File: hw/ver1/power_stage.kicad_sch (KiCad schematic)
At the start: 1 part, among them U3 74HC4051

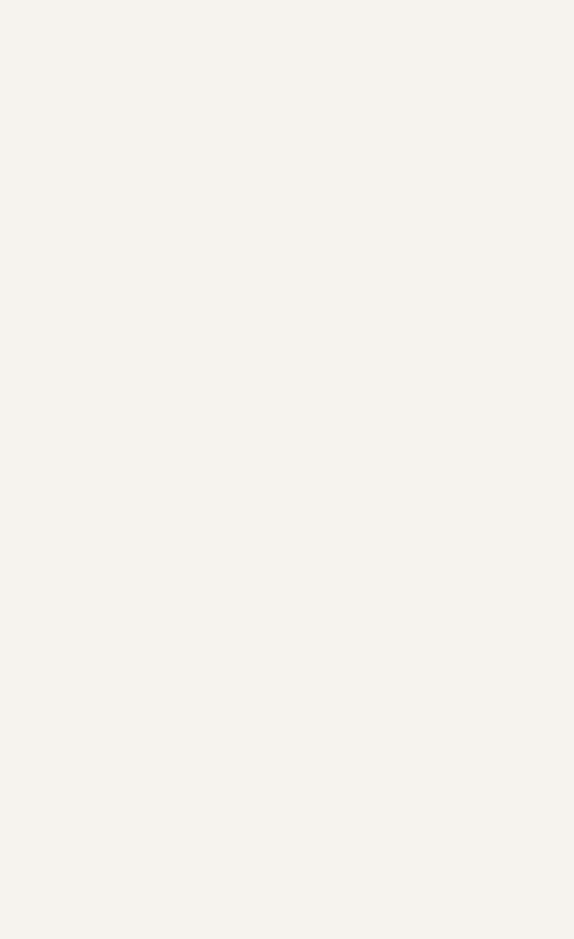
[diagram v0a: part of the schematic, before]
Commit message: Add virtual environment. Layout some schematic ideas. Add design doc for LTC7871.
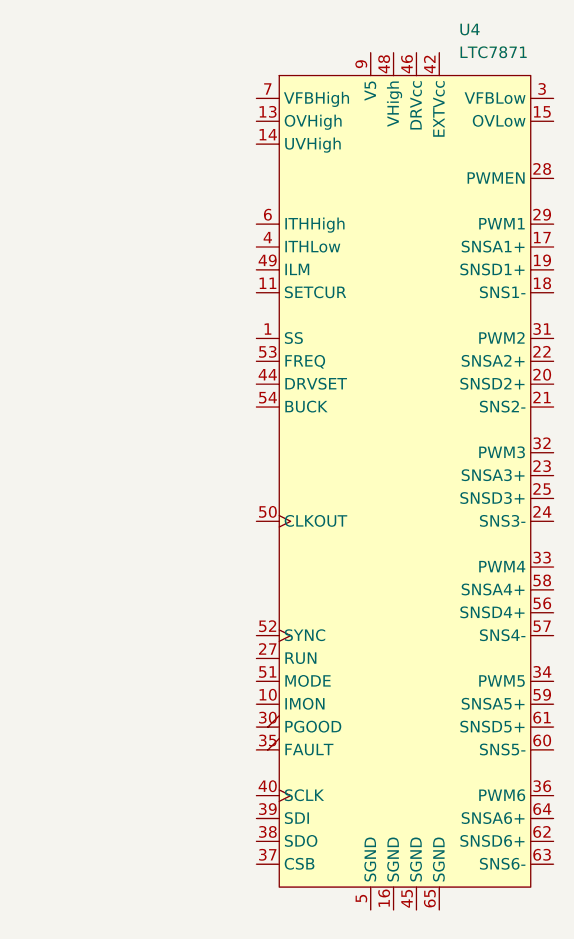
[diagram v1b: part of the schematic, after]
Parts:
- added U4: LTC7871, Package_QFP:LQFP-64-1EP_10x10mm_P0.5mm_EP6.5x6.5mm_ThermalVias, symbol ltc7871:LTC7871xLWE#xPBF

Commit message: Save the day's effort
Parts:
- added C1: 10uF, symbol Device:C
- added JP1: SolderJumper_2_Bridged, Jumper:SolderJumper-2_P1.3mm_Bridged_RoundedPad1.0x1.5mm, symbol Jumper:SolderJumper_2_Bridged
- added JP2: Jumper_3_Open, Jumper:SolderJumper-3_P1.3mm_Open_RoundedPad1.0x1.5mm_NumberLabels, symbol Jumper:Jumper_3_Open
- added R1: 1k, Resistor_SMD:R_0603_1608Metric, symbol Device:R_US
- added R2: 10k, Resistor_SMD:R_0603_1608Metric, symbol Device:R_US
- added TP1: TestPoint_Small, symbol Connector:TestPoint_Small
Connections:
- net GND: now reaches U4.16 (SGND)
- net GND: now also U4.45 (SGND), U4.5 (SGND), U4.65 (SGND), C1.2
- net LTC_RUN: now reaches U4.27 (RUN)
- net LTC_RUN: now also JP1.2 (B)
- net LTC_MODE: now reaches U4.51 (MODE)
- net LTC_MODE: now also JP2.2 (C)
- net +5P: now reaches U4.9 (V5)
- net +5P: now also C1.1, JP2.3 (B)
- new net: JP1.1 (A), R1.2, R2.2
- new net CTL_RUN: R1.1
- new net GNDD: JP2.1 (A), R2.1
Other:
- note added: "+5V == Discontinuous Mode GND == Forced Continuous Mode FLT == Burst Mode"

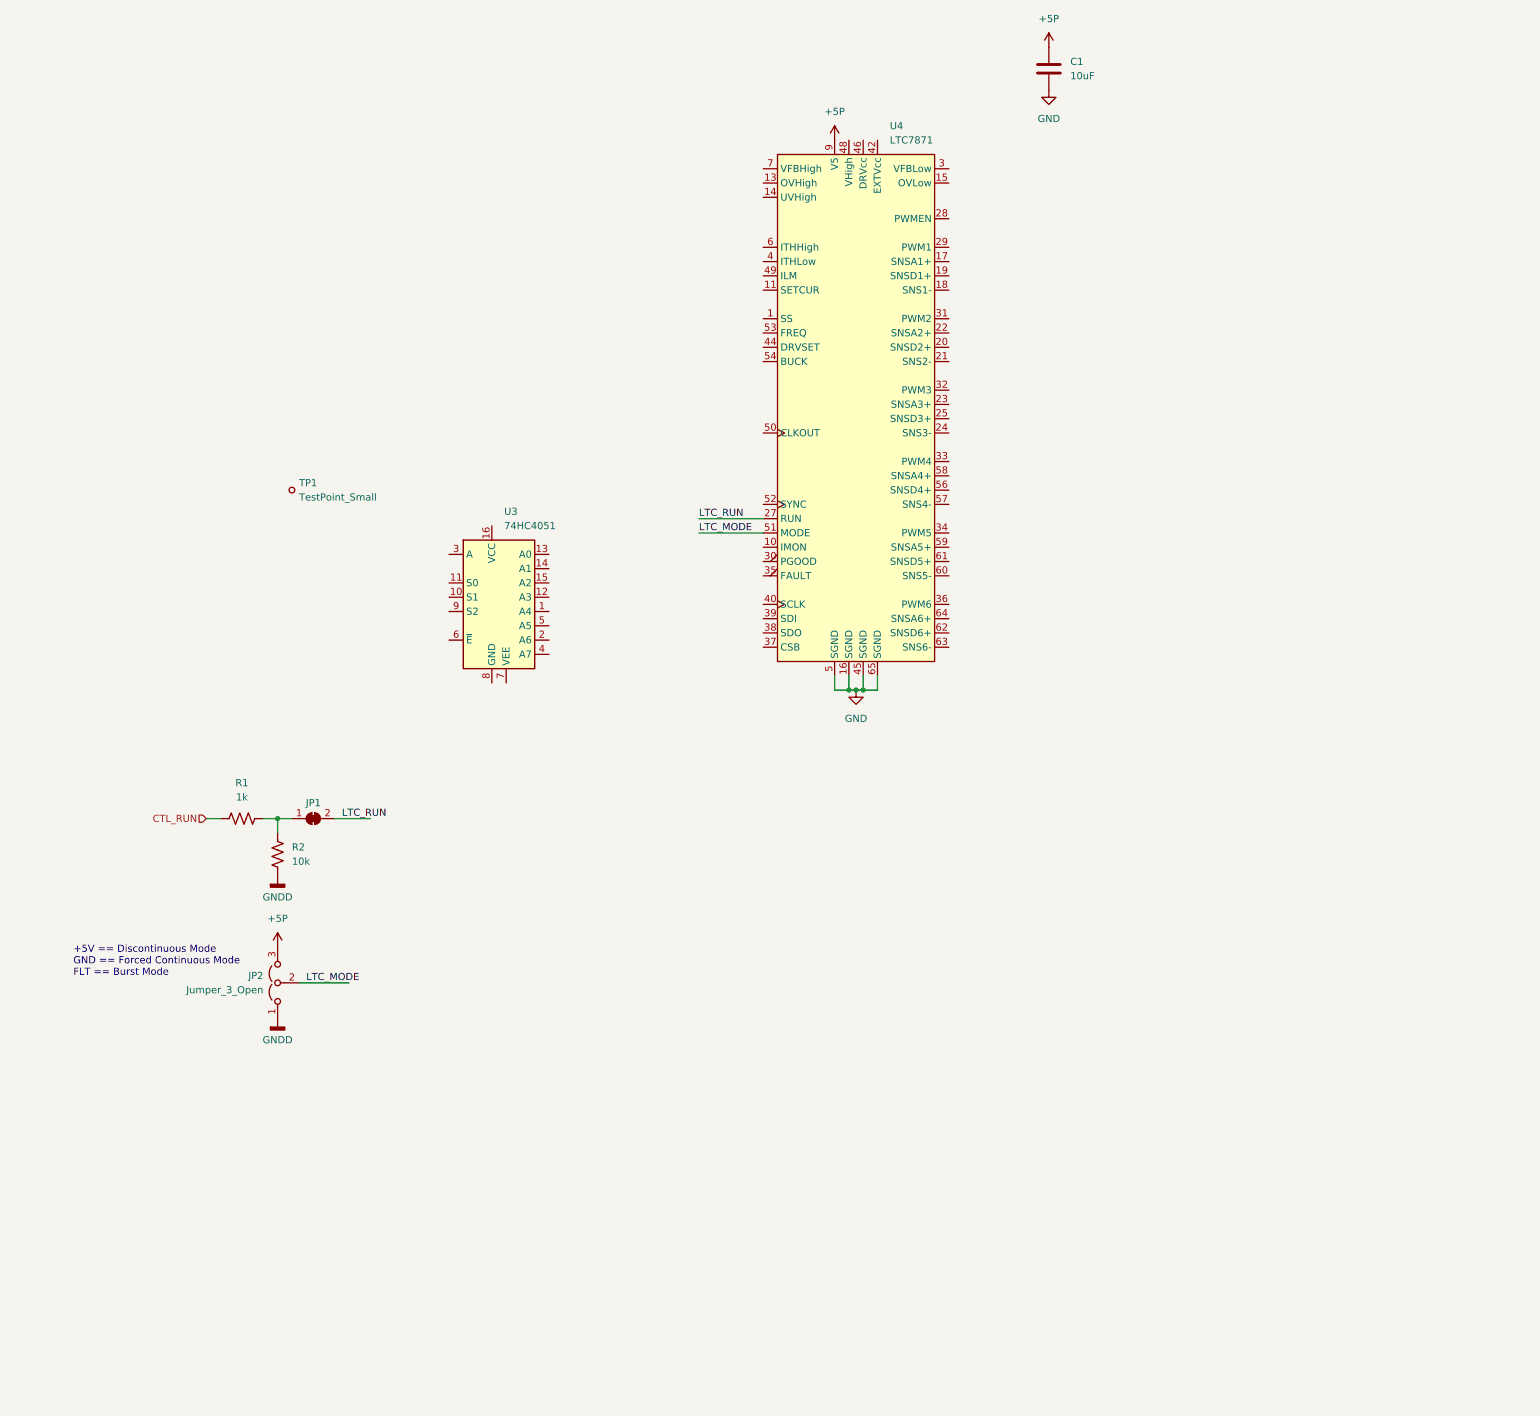
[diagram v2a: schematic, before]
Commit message: Flesh out some more of the power design
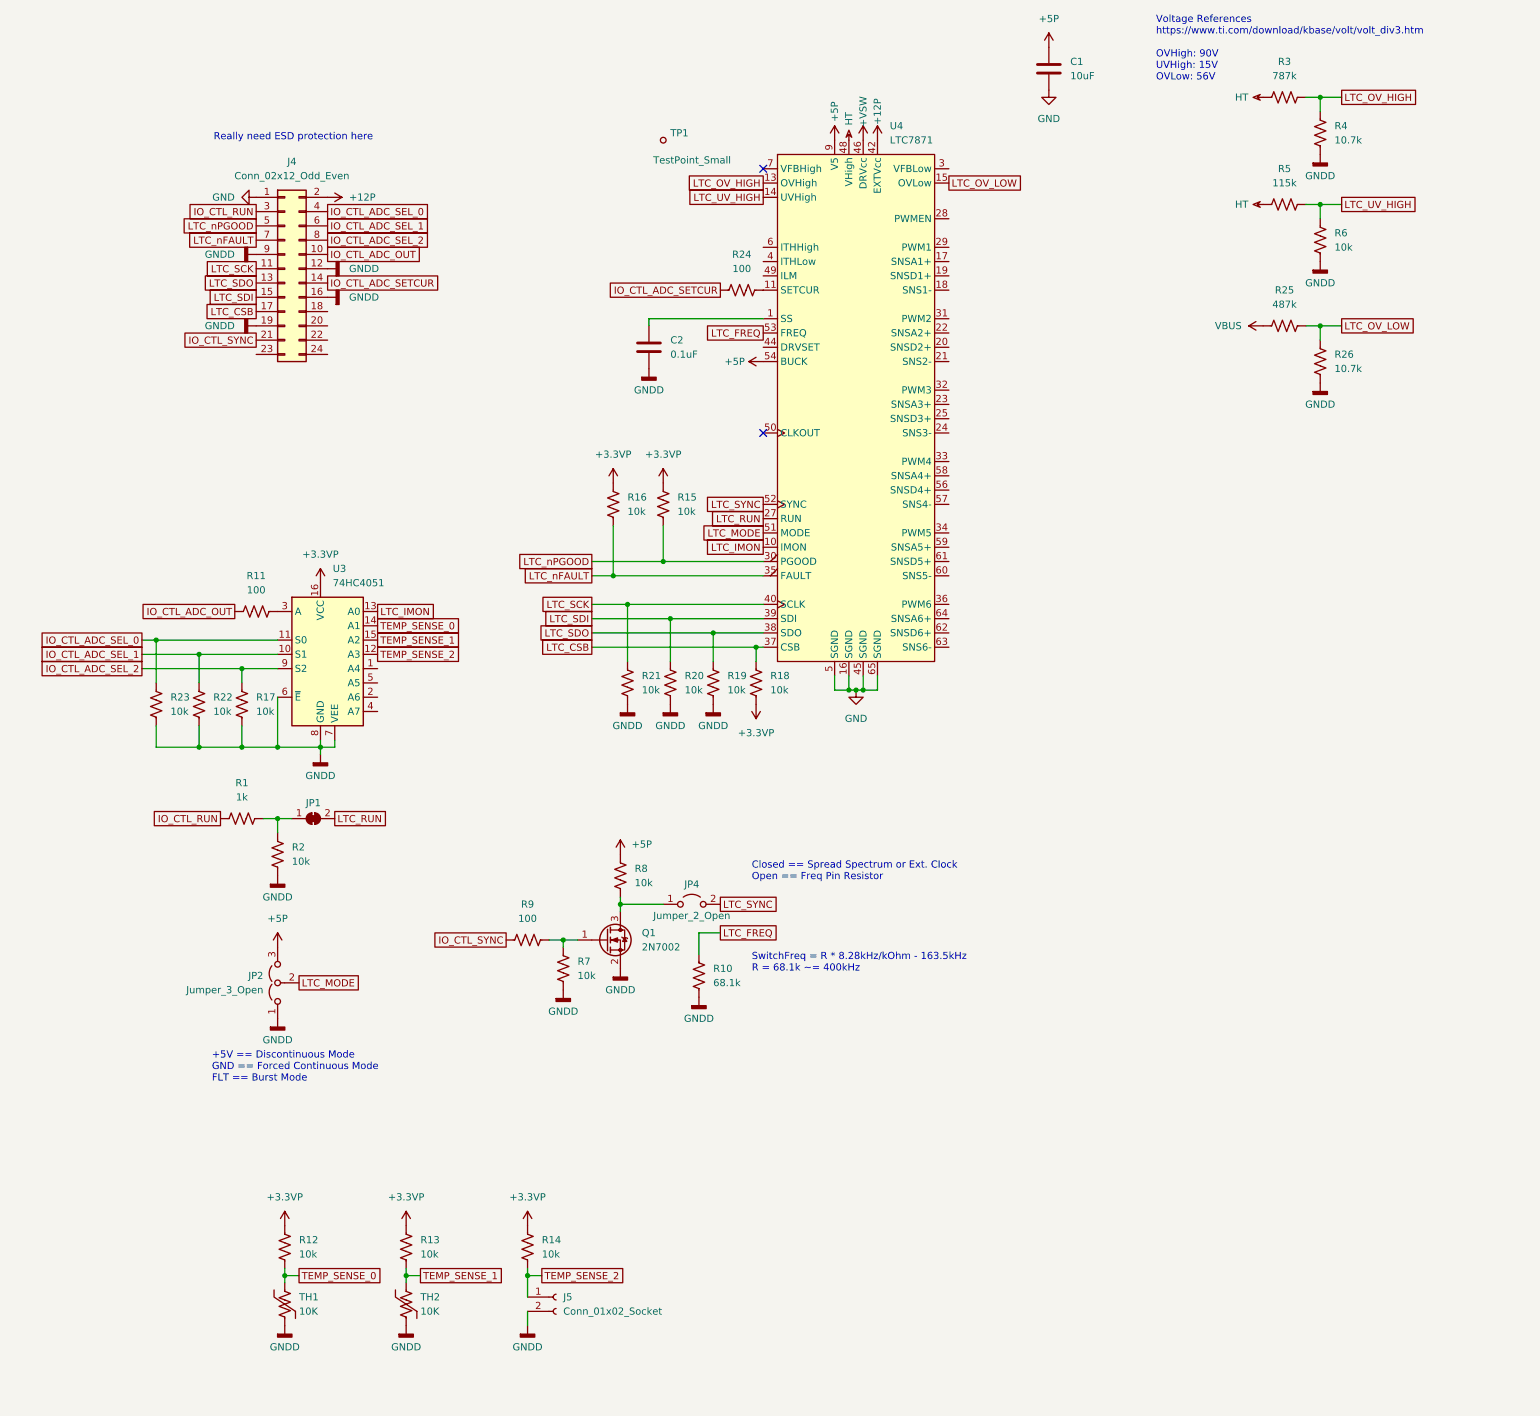
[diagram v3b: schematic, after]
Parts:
- added C2: 0.1uF, symbol Device:C
- added J4: Conn_02x12_Odd_Even, symbol Connector_Generic:Conn_02x12_Odd_Even
- added J5: Conn_01x02_Socket, symbol Connector:Conn_01x02_Socket
- added JP4: Jumper_2_Open, symbol Jumper:Jumper_2_Open
- added Q1: 2N7002, Package_TO_SOT_SMD:SOT-23, symbol Transistor_FET:2N7002
- added R10: 68.1k, Resistor_SMD:R_0603_1608Metric, symbol Device:R_US
- added R11, R24, R9: 100, Resistor_SMD:R_0603_1608Metric, symbol Device:R_US
- added R12, R13, R14, R15, R16, R17, R18, R19, R20, R21, R22, R23, R6, R7, R8: 10k, Resistor_SMD:R_0603_1608Metric, symbol Device:R_US
- added R25: 487k, Resistor_SMD:R_0603_1608Metric, symbol Device:R_US
- added R26, R4: 10.7k, Resistor_SMD:R_0603_1608Metric, symbol Device:R_US
- added R3: 787k, Resistor_SMD:R_0603_1608Metric, symbol Device:R_US
- added R5: 115k, Resistor_SMD:R_0603_1608Metric, symbol Device:R_US
- added TH1, TH2: 10K, symbol Device:Thermistor_US
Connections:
- net +5P: now also U4.54 (BUCK), R8.2
- net GND: now also J4.1 (Pin_1)
- net GNDD: now also U3.6 (~{E}), U3.7 (VEE), U3.8 (GND), C2.2, J4.12 (Pin_12), J4.16 (Pin_16), J4.19 (Pin_19), J4.9 (Pin_9), J5.2 (Pin_2), Q1.2 (S), R10.1, R17.1, R19.1, R20.1, R21.1, R22.1, R23.1, R26.1, R4.1, R6.1, R7.1, TH1.2, TH2.2
- net IO_CTL_ADC_SEL_1: now reaches U3.10 (S1)
- net IO_CTL_ADC_SEL_1: now also J4.6 (Pin_6), R22.2
- net IO_CTL_ADC_SEL_0: now reaches U3.11 (S0)
- net IO_CTL_ADC_SEL_0: now also J4.4 (Pin_4), R23.2
- net TEMP_SENSE_2: now reaches U3.12 (A3)
- net TEMP_SENSE_2: now also J5.1 (Pin_1), R14.1
- net LTC_IMON: now reaches U3.13 (A0)
- net LTC_IMON: now also U4.10 (IMON)
- net TEMP_SENSE_0: now reaches U3.14 (A1)
- net TEMP_SENSE_0: now also R12.1, TH1.1
- net TEMP_SENSE_1: now reaches U3.15 (A2)
- net TEMP_SENSE_1: now also R13.1, TH2.1
- net +3.3VP: now reaches U3.16 (VCC)
- net +3.3VP: now also R12.2, R13.2, R14.2, R15.2, R16.2, R18.1
- net at U3.3 (A): now also R11.2
- net IO_CTL_ADC_SEL_2: now reaches U3.9 (S2)
- net IO_CTL_ADC_SEL_2: now also J4.8 (Pin_8), R17.2
- net at U4.1 (SS): now also C2.1
- net at U4.11 (SETCUR): now also R24.2
- net LTC_OV_HIGH: now reaches U4.13 (OVHigh)
- net LTC_OV_HIGH: now also R3.2, R4.2
- net LTC_UV_HIGH: now reaches U4.14 (UVHigh)
- net LTC_UV_HIGH: now also R5.2, R6.2
- net LTC_OV_LOW: now reaches U4.15 (OVLow)
- net LTC_OV_LOW: now also R25.2, R26.2
- net LTC_nPGOOD: now reaches U4.30 (PGOOD)
- net LTC_nPGOOD: now also J4.5 (Pin_5), R15.1
- net LTC_nFAULT: now reaches U4.35 (FAULT)
- net LTC_nFAULT: now also J4.7 (Pin_7), R16.1
- net LTC_CSB: now reaches U4.37 (CSB)
- net LTC_CSB: now also J4.17 (Pin_17), R18.2
- net LTC_SDO: now reaches U4.38 (SDO)
- net LTC_SDO: now also J4.13 (Pin_13), R19.2
- net LTC_SDI: now reaches U4.39 (SDI)
- net LTC_SDI: now also J4.15 (Pin_15), R20.2
- net LTC_SCK: now reaches U4.40 (SCLK)
- net LTC_SCK: now also J4.11 (Pin_11), R21.2
- net +12P: now reaches U4.42 (EXTVcc)
- net +12P: now also J4.2 (Pin_2)
- net +VSW: now reaches U4.46 (DRVcc)
- net HT: now reaches U4.48 (VHigh)
- net HT: now also R3.1, R5.1
- net LTC_SYNC: now reaches U4.52 (SYNC)
- net LTC_SYNC: now also JP4.2 (B)
- net LTC_FREQ: now reaches U4.53 (FREQ)
- net LTC_FREQ: now also R10.2
- net CTL_RUN renamed IO_CTL_RUN
- net IO_CTL_RUN: now also J4.3 (Pin_3)
- new net: Q1.1 (G), R7.2, R9.1
- new net: JP4.1 (A), Q1.3 (D), R8.1
- new net IO_CTL_ADC_OUT: J4.10 (Pin_10), R11.1
- new net IO_CTL_ADC_SETCUR: J4.14 (Pin_14), R24.1
- new net IO_CTL_SYNC: J4.21 (Pin_21), R9.2
- new net VBUS: R25.1
- no-connect marks 0 -> 2
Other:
- note added: "Closed == Spread Spectrum or Ext. Clock Open == Freq Pin Resistor"
- note added: "Really need ESD protection here"
- note added: "SwitchFreq = R * 8.28kHz/kOhm - 163.5kHz R = 68.1k ~= 400kHz"
- note added: "Voltage References https://www.ti.com/download/kbase/volt/volt_div3.htm OVHigh: 90V UVHigh: 15V OVLow: 56V"
- moved on the sheet: TP1, U3

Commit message: Save lunch work
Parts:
- added C10: Cff, symbol Device:C
- added C3, C5, C9: 0.1uF, symbol Device:C
- added C4: 10uF, symbol Device:C
- added C6: 0.33uF, symbol Device:C
- added C7: 1nF, symbol Device:C
- added C8: 47pF, symbol Device:C
- added R27, R28, R31: 10k, Resistor_SMD:R_0603_1608Metric, symbol Device:R_US
- added R29, R30: 499, Resistor_SMD:R_0603_1608Metric, symbol Device:R_US
- added R32: 100k, Resistor_SMD:R_0603_1608Metric, symbol Device:R_US
- added R33: 160k, Resistor_SMD:R_0603_1608Metric, symbol Device:R_US
- added R34: 325k, Resistor_SMD:R_0603_1608Metric, symbol Device:R_US
- added SW1: SW_DIP_x03, symbol Switch:SW_DIP_x03
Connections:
- net +5P: now also U4.44 (DRVSET), C3.1, R27.2
- net +VSW: now also C4.1, C5.1
- net GND: now also C3.2, C4.2, C5.2
- net GNDD: now also C7.2, C8.2, R28.1, R29.1, R30.1, R31.1
- net VBUS: now also C10.1, R32.2, R33.2, R34.2
- net LTC_SETCUR: now reaches R24.2, U4.11 (SETCUR)
- net LTC_VFB_LOW: now reaches U4.3 (VFBLow)
- net LTC_VFB_LOW: now also C10.2, R31.2, SW1.4, SW1.5, SW1.6
- net LTC_ITH_LOW: now reaches U4.4 (ITHLow)
- net LTC_ITH_LOW: now also C8.1, C9.1
- net LTC_ILIM: now reaches U4.49 (ILM)
- net LTC_ILIM: now also R27.1, R28.2
- net LTC_ITH_HIGH: now reaches U4.6 (ITHHigh)
- net LTC_ITH_HIGH: now also C6.1, C7.1
- new net: R33.1, SW1.2
- new net: C9.2, R30.2
- new net: R34.1, SW1.1
- new net: R32.1, SW1.3
- new net: C6.2, R29.2
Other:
- note added: "Current comparator compensation"
- note added: "DRVcc bypass. Place close to pin."
- note added: "From ltc7871.ipynb, 1kW, 4phase output DCR Sense 30mV"
- note added: "From ltc7871.ipynb. Selects 12v, 24v, and 48v nominal voltages. Add graphical table on back of board."
- note added: "V5 bypass. Place close to pin."
- moved on the sheet: C1, J4, R24
